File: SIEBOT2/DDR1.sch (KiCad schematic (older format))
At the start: 17 parts, among them U2 MT46V32M16TG, U3 M25P32

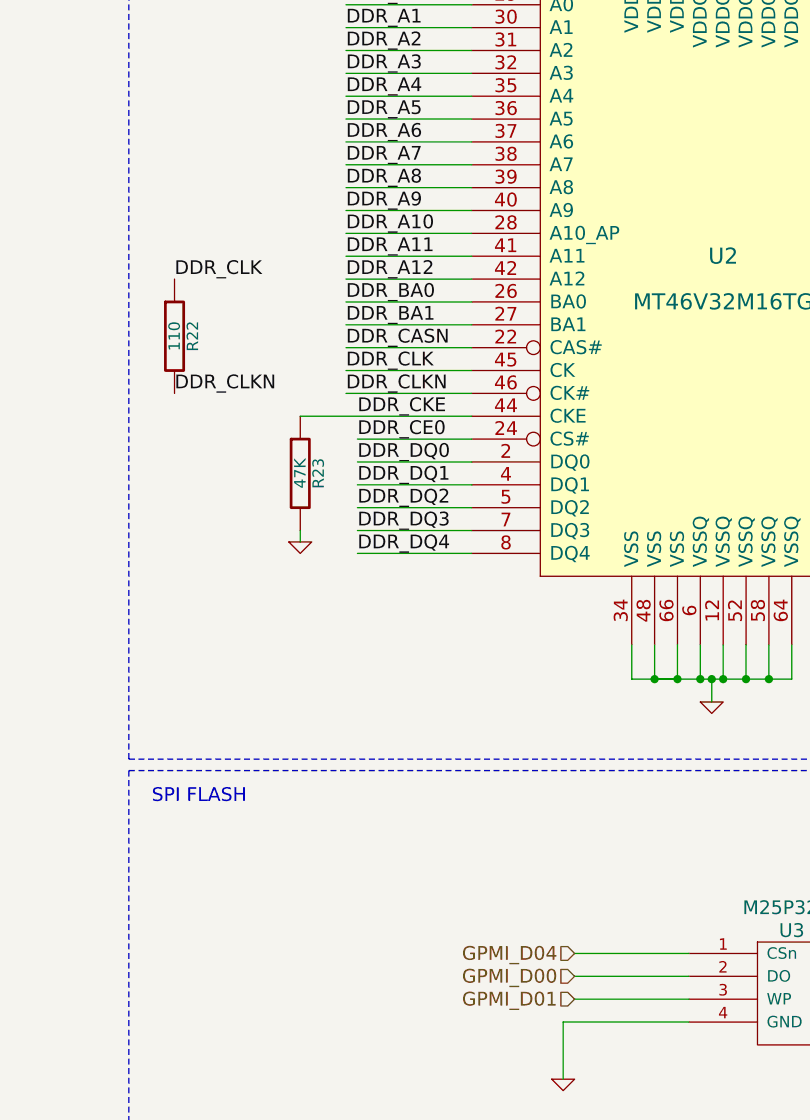
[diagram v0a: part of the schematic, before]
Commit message: Added some fixes from AndroidStamp
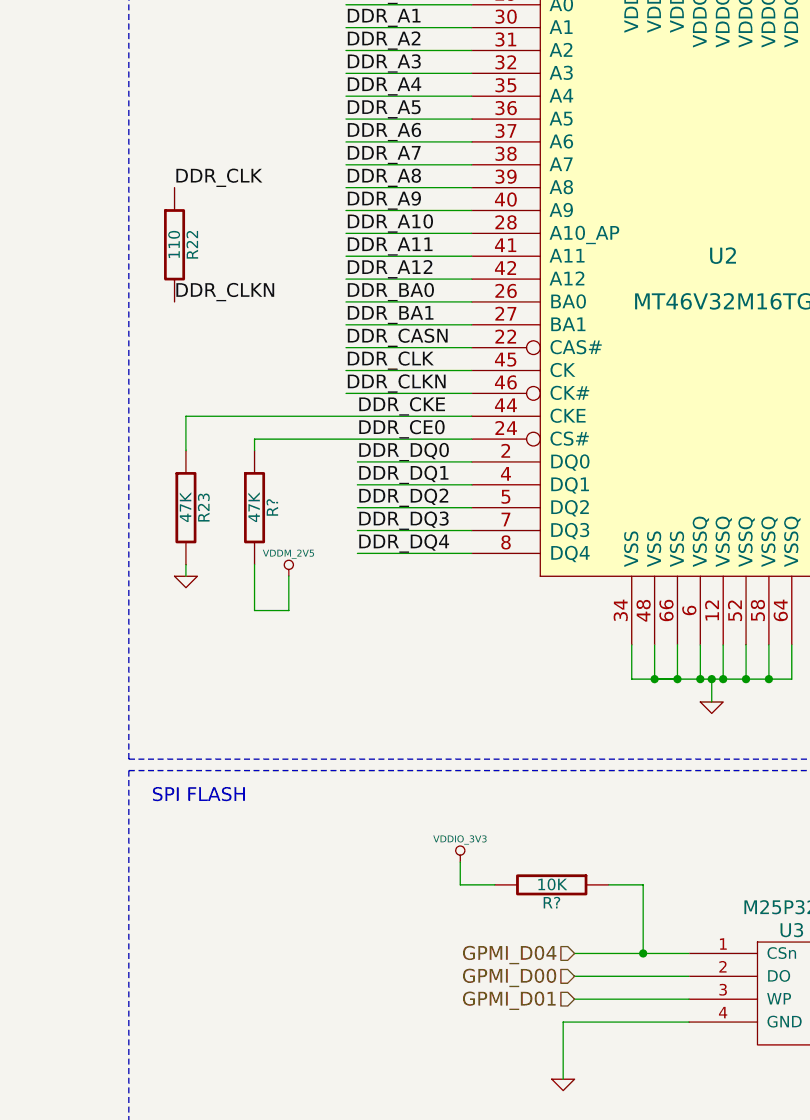
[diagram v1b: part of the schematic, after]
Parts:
- added R?: 47K, symbol R
- added R?: 10K, symbol R
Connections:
- wire segments 136 -> 145
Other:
- moved on the sheet: R22, R23
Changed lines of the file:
@@
-EESchema Schematic File Version 2  date sáb 05 mar 2011 23:35:11 COT
+EESchema Schematic File Version 2  date jue 07 abr 2011 23:57:53 COT
 LIBS:stm32f100vxx
 LIBS:transistor-npn
@@
 LIBS:PROpendous-cache
 LIBS:w_analog
+LIBS:adm3101e
 LIBS:i.mx233stamp-cache
 EELAYER 25  0
@@
 Sheet 5 6
 Title ""
-Date "6 mar 2011"
+Date "8 apr 2011"
 Rev ""
 Comp ""
@@
 Comment4 ""
 $EndDescr
-Text Notes 5850 5500 0    60   ~ 0
-SPI FLASH
+Wire Wire Line
+	7700 6250 8200 6250
+Connection ~ 8000 6150
+Wire Wire Line
+	8000 6150 8000 5850
+Wire Wire Line
+	8000 5850 7850 5850
+Wire Wire Line
+	7250 3900 6300 3900
+Wire Wire Line
+	6300 3900 6300 3950
 Wire Notes Line
 	5750 5350 5750 7150
@@
 Wire Wire Line
 	6700 3300 7250 3300
-Wire Wire Line
-	7250 3800 6500 3800
 Connection ~ 10800 1500
 Wire Wire Line
@@
 Connection ~ 9600 950
 Connection ~ 9900 950
-Wire Wire Line
-	9850 6350 9350 6350
 Wire Wire Line
 	9700 6000 9700 6150
@@
 Connection ~ 8450 1500
 Wire Wire Line
-	7700 6250 8200 6250
-Wire Wire Line
 	8200 6450 7650 6450
 Wire Wire Line
@@
 Connection ~ 10800 2700
 Wire Wire Line
-	6500 4300 6500 4350
+	6000 4450 6000 4500
 Wire Wire Line
 	6700 3400 7250 3400
@@
 	6700 3600 7250 3600
 Wire Wire Line
-	6750 3900 7250 3900
-Wire Wire Line
 	9450 3400 10000 3400
 Wire Wire Line
@@
 Wire Notes Line
 	11150 7150 5750 7150
+Wire Wire Line
+	6000 3950 6000 3800
+Wire Wire Line
+	6000 3800 7250 3800
+Wire Wire Line
+	6300 4450 6300 4650
+Wire Wire Line
+	6300 4650 6450 4650
+Wire Wire Line
+	6450 4650 6450 4500
+Wire Wire Line
+	7200 5750 7200 5850
+Wire Wire Line
+	7200 5850 7350 5850
+Wire Wire Line
+	9850 6350 9350 6350
+$Comp
+L VDDIO_3V3 #PWR?
+U 1 1 4D7D59A9
+P 7200 5750
+F 0 "#PWR?" H 7200 5850 30  0001 C CNN
+F 1 "VDDIO_3V3" H 7200 5850 30  0000 C CNN
+	1    7200 5750
+	1    0    0    -1
+$EndComp
+$Comp
+L R R?
+U 1 1 4D7D5980
+P 7600 5850
+F 0 "R?" V 7680 5850 50  0000 C CNN
+F 1 "10K" V 7600 5850 50  0000 C CNN
+	1    7600 5850
+	0    1    1    0
+$EndComp
+$Comp
+L VDDM_2V5 #PWR?
+U 1 1 4D7D4B15
+P 6450 4500
+F 0 "#PWR?" H 6450 4600 30  0001 C CNN
+F 1 "VDDM_2V5" H 6450 4600 30  0000 C CNN
+	1    6450 4500
+	1    0    0    -1
+$EndComp
+$Comp
+L R R?
+U 1 1 4D7D4AD6
+P 6300 4200
+F 0 "R?" V 6380 4200 50  0000 C CNN
+F 1 "47K" V 6300 4200 50  0000 C CNN
+	1    6300 4200
+	1    0    0    -1
+$EndComp
+Text Notes 5850 5500 0    60   ~ 0
+SPI FLASH
 Text Notes 5850 750  0    60   ~ 0
 DDR RAM
-Text Label 5950 3700 0    60   ~ 0
+Text Label 5950 3300 0    60   ~ 0
 DDR_CLKN
-Text Label 5950 3200 0    60   ~ 0
+Text Label 5950 2800 0    60   ~ 0
 DDR_CLK
 $Comp
 L R R22
 U 1 1 4D41DFB8
-P 5950 3450
-F 0 "R22" V 6030 3450 50  0000 C CNN
-F 1 "110" V 5950 3450 50  0000 C CNN
-	1    5950 3450
+P 5950 3050
+F 0 "R22" V 6030 3050 50  0000 C CNN
+F 1 "110" V 5950 3050 50  0000 C CNN
+	1    5950 3050
 	1    0    0    -1
 $EndComp
@@
 L R R23
 U 1 1 4D418363
-P 6500 4050
-F 0 "R23" V 6580 4050 50  0000 C CNN
-F 1 "47K" V 6500 4050 50  0000 C CNN
-	1    6500 4050
+P 6000 4200
+F 0 "R23" V 6080 4200 50  0000 C CNN
+F 1 "47K" V 6000 4200 50  0000 C CNN
+	1    6000 4200
 	1    0    0    -1
 $EndComp
@@
 L GND #PWR01
 U 1 1 4D418353
-P 6500 4350
-F 0 "#PWR01" H 6500 4350 30  0001 C CNN
-F 1 "GND" H 6500 4280 30  0001 C CNN
-	1    6500 4350
+P 6000 4500
+F 0 "#PWR01" H 6000 4500 30  0001 C CNN
+F 1 "GND" H 6000 4430 30  0001 C CNN
+	1    6000 4500
 	1    0    0    -1
 $EndComp

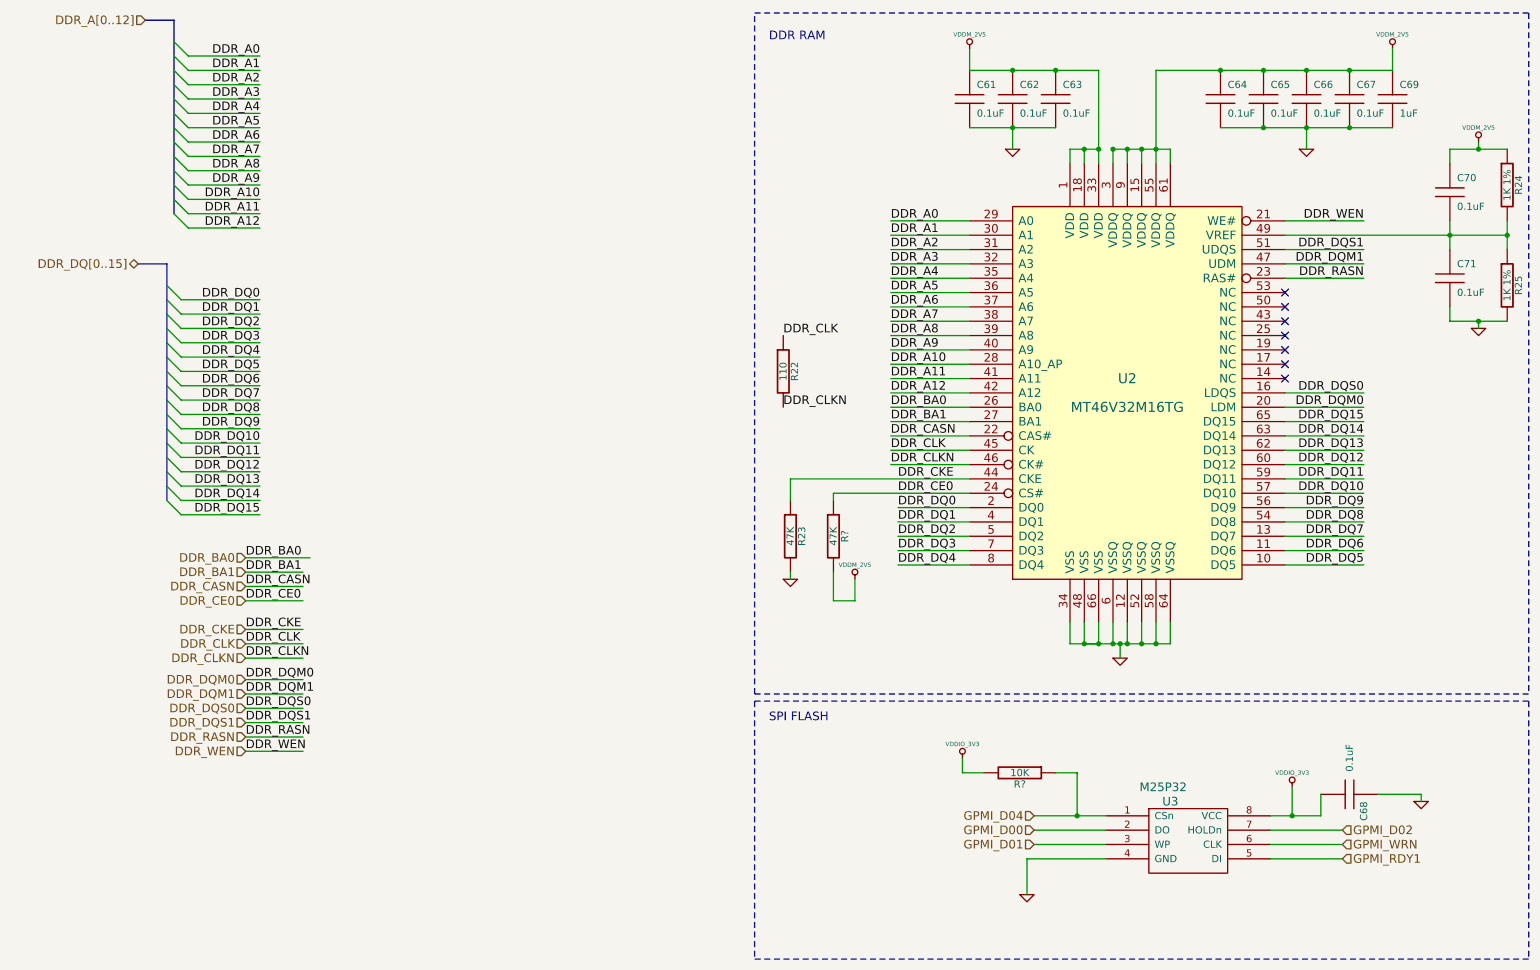
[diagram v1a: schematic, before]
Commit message: Added power dc-dc, fixed stm32 control pins
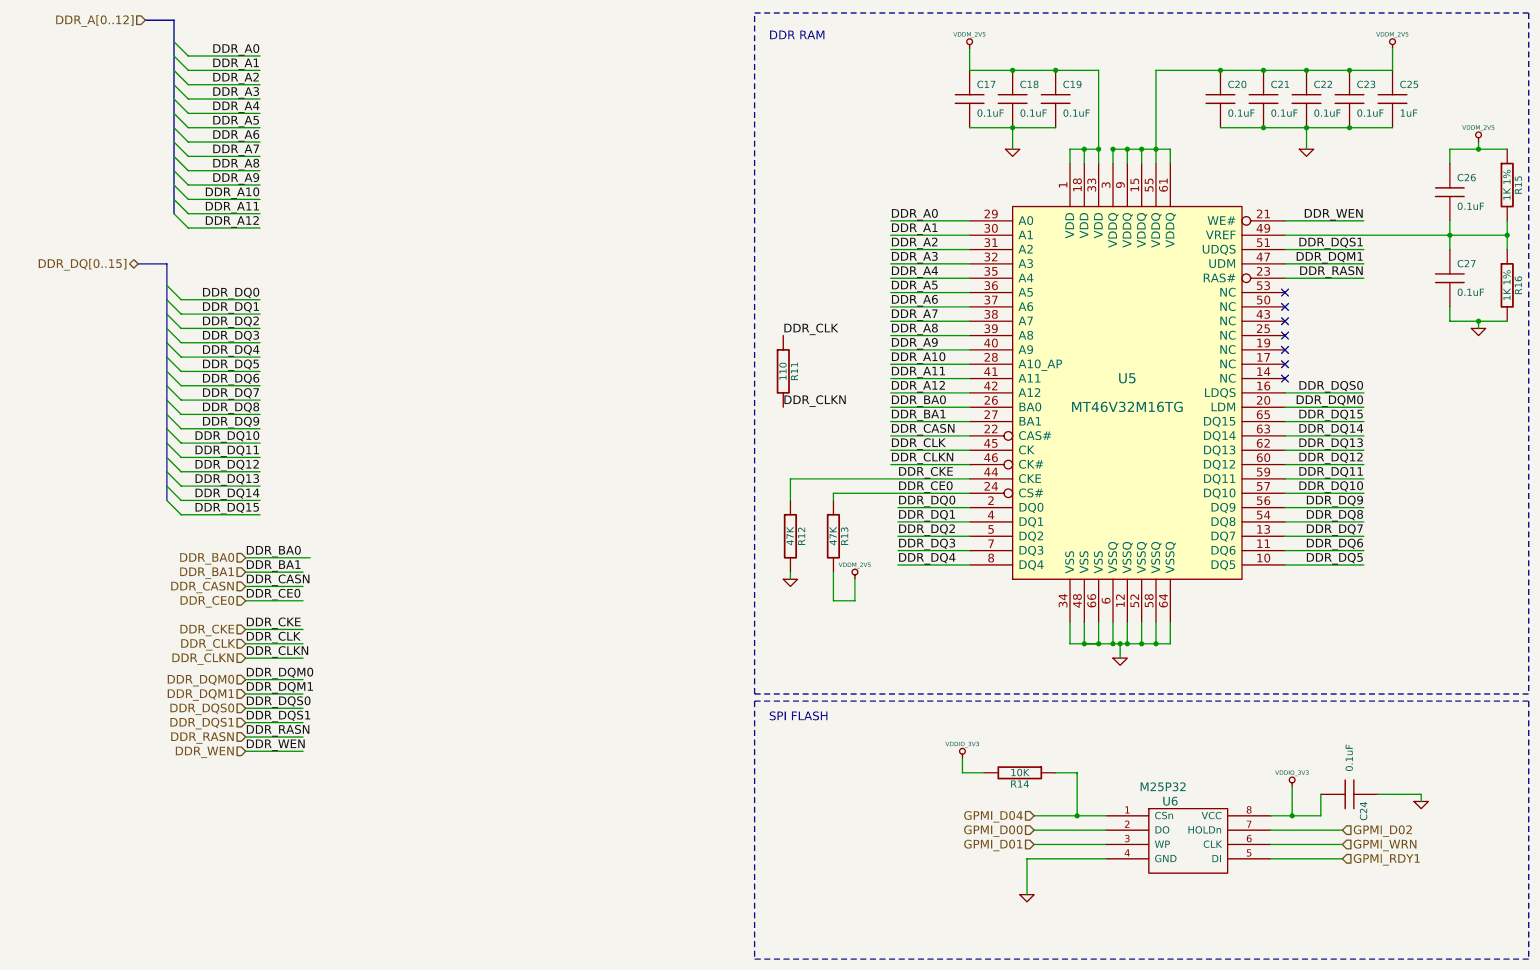
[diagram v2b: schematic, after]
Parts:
- gave numbers to parts that had none: 2
- renumbered C61 to C17, C62 to C18, C63 to C19, C64 to C20, C65 to C21, C66 to C22, C67 to C23, C68 to C24, C69 to C25, C70 to C26, C71 to C27, R22 to R11, R23 to R12, R24 to R15, R25 to R16, U2 to U5, U3 to U6
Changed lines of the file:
@@
-EESchema Schematic File Version 2  date jue 07 abr 2011 23:57:53 COT
+EESchema Schematic File Version 2  date lun 11 abr 2011 13:13:06 COT
+LIBS:dc-dc
 LIBS:stm32f100vxx
 LIBS:transistor-npn
@@
 Sheet 5 6
 Title ""
-Date "8 apr 2011"
+Date "11 apr 2011"
 Rev ""
 Comp ""
@@
 	9850 6350 9350 6350
 $Comp
-L VDDIO_3V3 #PWR?
+L VDDIO_3V3 #PWR049
 U 1 1 4D7D59A9
 P 7200 5750
-F 0 "#PWR?" H 7200 5850 30  0001 C CNN
+F 0 "#PWR049" H 7200 5850 30  0001 C CNN
 F 1 "VDDIO_3V3" H 7200 5850 30  0000 C CNN
 	1    7200 5750
@@
 $EndComp
 $Comp
-L R R?
+L R R14
 U 1 1 4D7D5980
 P 7600 5850
-F 0 "R?" V 7680 5850 50  0000 C CNN
+F 0 "R14" V 7680 5850 50  0000 C CNN
 F 1 "10K" V 7600 5850 50  0000 C CNN
 	1    7600 5850
@@
 $EndComp
 $Comp
-L VDDM_2V5 #PWR?
+L VDDM_2V5 #PWR050
 U 1 1 4D7D4B15
 P 6450 4500
-F 0 "#PWR?" H 6450 4600 30  0001 C CNN
+F 0 "#PWR050" H 6450 4600 30  0001 C CNN
 F 1 "VDDM_2V5" H 6450 4600 30  0000 C CNN
 	1    6450 4500
@@
 $EndComp
 $Comp
-L R R?
+L R R13
 U 1 1 4D7D4AD6
 P 6300 4200
-F 0 "R?" V 6380 4200 50  0000 C CNN
+F 0 "R13" V 6380 4200 50  0000 C CNN
 F 1 "47K" V 6300 4200 50  0000 C CNN
 	1    6300 4200
@@
 DDR_CLK
 $Comp
-L R R22
+L R R11
 U 1 1 4D41DFB8
 P 5950 3050
-F 0 "R22" V 6030 3050 50  0000 C CNN
+F 0 "R11" V 6030 3050 50  0000 C CNN
 F 1 "110" V 5950 3050 50  0000 C CNN
 	1    5950 3050
@@
 DDR_CASN
 $Comp
-L R R23
+L R R12
 U 1 1 4D418363
 P 6000 4200
-F 0 "R23" V 6080 4200 50  0000 C CNN
+F 0 "R12" V 6080 4200 50  0000 C CNN
 F 1 "47K" V 6000 4200 50  0000 C CNN
 	1    6000 4200
@@
 $EndComp
 $Comp
-L GND #PWR01
+L GND #PWR051
 U 1 1 4D418353
 P 6000 4500
-F 0 "#PWR01" H 6000 4500 30  0001 C CNN
+F 0 "#PWR051" H 6000 4500 30  0001 C CNN
 F 1 "GND" H 6000 4430 30  0001 C CNN
 	1    6000 4500
@@
 DDR_CKE
 $Comp
-L GND #PWR02
+L GND #PWR052
 U 1 1 4D417AF1
 P 10800 2750
-F 0 "#PWR02" H 10800 2750 30  0001 C CNN
+F 0 "#PWR052" H 10800 2750 30  0001 C CNN
 F 1 "GND" H 10800 2680 30  0001 C CNN
 	1    10800 2750
@@
 $EndComp
 $Comp
-L VDDM_2V5 #PWR03
+L VDDM_2V5 #PWR053
 U 1 1 4D417ACD
 P 10800 1450
-F 0 "#PWR03" H 10800 1550 30  0001 C CNN
+F 0 "#PWR053" H 10800 1550 30  0001 C CNN
 F 1 "VDDM_2V5" H 10800 1550 30  0000 C CNN
 	1    10800 1450
@@
 $EndComp
 $Comp
-L R R25
+L R R16
 U 1 1 4D417AA2
 P 11000 2450
-F 0 "R25" V 11080 2450 50  0000 C CNN
+F 0 "R16" V 11080 2450 50  0000 C CNN
 F 1 "1K 1%" V 11000 2450 50  0000 C CNN
 	1    11000 2450
@@
 $EndComp
 $Comp
-L R R24
+L R R15
 U 1 1 4D417A9C
 P 11000 1750
-F 0 "R24" V 11080 1750 50  0000 C CNN
+F 0 "R15" V 11080 1750 50  0000 C CNN
 F 1 "1K 1%" V 11000 1750 50  0000 C CNN
 	1    11000 1750
@@
 $EndComp
 $Comp
-L C C71
+L C C27
 U 1 1 4D417A94
 P 10600 2400
-F 0 "C71" H 10650 2500 50  0000 L CNN
+F 0 "C27" H 10650 2500 50  0000 L CNN
 F 1 "0.1uF" H 10650 2300 50  0000 L CNN
 	1    10600 2400
@@
 $EndComp
 $Comp
-L C C70
+L C C26
 U 1 1 4D417A8B
 P 10600 1800
-F 0 "C70" H 10650 1900 50  0000 L CNN
+F 0 "C26" H 10650 1900 50  0000 L CNN
 F 1 "0.1uF" H 10650 1700 50  0000 L CNN
 	1    10600 1800
@@
 $EndComp
 $Comp
-L VDDM_2V5 #PWR04
+L VDDM_2V5 #PWR054
 U 1 1 4D4179A4
 P 7250 800
-F 0 "#PWR04" H 7250 900 30  0001 C CNN
+F 0 "#PWR054" H 7250 900 30  0001 C CNN
 F 1 "VDDM_2V5" H 7250 900 30  0000 C CNN
 	1    7250 800
@@
 $EndComp
 $Comp
-L VDDM_2V5 #PWR05
+L VDDM_2V5 #PWR055
 U 1 1 4D417999
 P 10200 800
-F 0 "#PWR05" H 10200 900 30  0001 C CNN
+F 0 "#PWR055" H 10200 900 30  0001 C CNN
 F 1 "VDDM_2V5" H 10200 900 30  0000 C CNN
 	1    10200 800
@@
 $EndComp
 $Comp
-L GND #PWR06
+L GND #PWR056
 U 1 1 4D41792B
 P 7550 1500
-F 0 "#PWR06" H 7550 1500 30  0001 C CNN
+F 0 "#PWR056" H 7550 1500 30  0001 C CNN
 F 1 "GND" H 7550 1430 30  0001 C CNN
 	1    7550 1500
@@
 $EndComp
 $Comp
-L C C61
+L C C17
 U 1 1 4D417911
 P 7250 1150
-F 0 "C61" H 7300 1250 50  0000 L CNN
+F 0 "C17" H 7300 1250 50  0000 L CNN
 F 1 "0.1uF" H 7300 1050 50  0000 L CNN
 	1    7250 1150
@@
 $EndComp
 $Comp
-L C C62
+L C C18
 U 1 1 4D41790C
 P 7550 1150
-F 0 "C62" H 7600 1250 50  0000 L CNN
+F 0 "C18" H 7600 1250 50  0000 L CNN
 F 1 "0.1uF" H 7600 1050 50  0000 L CNN
 	1    7550 1150
@@
 $EndComp
 $Comp
-L C C63
+L C C19
 U 1 1 4D417905
 P 7850 1150
-F 0 "C63" H 7900 1250 50  0000 L CNN
+F 0 "C19" H 7900 1250 50  0000 L CNN
 F 1 "0.1uF" H 7900 1050 50  0000 L CNN
 	1    7850 1150
@@
 $EndComp
 $Comp
-L GND #PWR07
+L GND #PWR057
 U 1 1 4D417882
 P 9600 1500
-F 0 "#PWR07" H 9600 1500 30  0001 C CNN
+F 0 "#PWR057" H 9600 1500 30  0001 C CNN
 F 1 "GND" H 9600 1430 30  0001 C CNN
 	1    9600 1500
@@
 $EndComp
 $Comp
-L C C69
+L C C25
 U 1 1 4D417845
 P 10200 1150
-F 0 "C69" H 10250 1250 50  0000 L CNN
+F 0 "C25" H 10250 1250 50  0000 L CNN
 F 1 "1uF" H 10250 1050 50  0000 L CNN
 	1    10200 1150
@@
 $EndComp
 $Comp
-L C C67
+L C C23
 U 1 1 4D41783A
 P 9900 1150
-F 0 "C67" H 9950 1250 50  0000 L CNN
+F 0 "C23" H 9950 1250 50  0000 L CNN
 F 1 "0.1uF" H 9950 1050 50  0000 L CNN
 	1    9900 1150
@@
 $EndComp
 $Comp
-L C C66
+L C C22
 U 1 1 4D417834
 P 9600 1150
-F 0 "C66" H 9650 1250 50  0000 L CNN
+F 0 "C22" H 9650 1250 50  0000 L CNN
 F 1 "0.1uF" H 9650 1050 50  0000 L CNN
 	1    9600 1150
@@
 $EndComp
 $Comp
-L C C65
+L C C21
 U 1 1 4D41782F
 P 9300 1150
-F 0 "C65" H 9350 1250 50  0000 L CNN
+F 0 "C21" H 9350 1250 50  0000 L CNN
 F 1 "0.1uF" H 9350 1050 50  0000 L CNN
 	1    9300 1150
@@
 $EndComp
 $Comp
-L C C64
+L C C20
 U 1 1 4D417828
 P 9000 1150
-F 0 "C64" H 9050 1250 50  0000 L CNN
+F 0 "C20" H 9050 1250 50  0000 L CNN
 F 1 "0.1uF" H 9050 1050 50  0000 L CNN
 	1    9000 1150
@@
 GPMI_D04
 $Comp
-L GND #PWR08
+L GND #PWR058
 U 1 1 4D409664
 P 10400 6050
-F 0 "#PWR08" H 10400 6050 30  0001 C CNN
+F 0 "#PWR058" H 10400 6050 30  0001 C CNN
 F 1 "GND" H 10400 5980 30  0001 C CNN
 	1    10400 6050
@@
 $EndComp
 $Comp
-L C C68
+L C C24
 U 1 1 4D409658
 P 9900 6000
-F 0 "C68" H 9950 6100 50  0000 L CNN
+F 0 "C24" H 9950 6100 50  0000 L CNN
 F 1 "0.1uF" H 9550 6000 50  0000 L CNN
 	1    9900 6000
@@
 $EndComp
 $Comp
-L VDDIO_3V3 #PWR09
+L VDDIO_3V3 #PWR059
 U 1 1 4D409635
 P 9500 5950
-F 0 "#PWR09" H 9500 6050 30  0001 C CNN
+F 0 "#PWR059" H 9500 6050 30  0001 C CNN
 F 1 "VDDIO_3V3" H 9500 6050 30  0000 C CNN
 	1    9500 5950
@@
 $EndComp
 $Comp
-L GND #PWR010
+L GND #PWR060
 U 1 1 4D409619
 P 7650 6700
-F 0 "#PWR010" H 7650 6700 30  0001 C CNN
+F 0 "#PWR060" H 7650 6700 30  0001 C CNN
 F 1 "GND" H 7650 6630 30  0001 C CNN
 	1    7650 6700
@@
 $EndComp
 $Comp
-L M25P32 U3
+L M25P32 U6
 U 1 1 4D40953F
 P 8800 6200
-F 0 "U3" H 8650 6350 60  0000 C CNN
+F 0 "U6" H 8650 6350 60  0000 C CNN
 F 1 "M25P32" H 8600 6450 60  0000 C CNN
 	1    8800 6200
@@
 DDR_WEN
 $Comp
-L GND #PWR011
+L GND #PWR061
 U 1 1 4D319D50
 P 8300 5050
-F 0 "#PWR011" H 8300 5050 30  0001 C CNN
+F 0 "#PWR061" H 8300 5050 30  0001 C CNN
 F 1 "GND" H 8300 4980 30  0001 C CNN
 	1    8300 5050
@@
 	1700 750  1800 850
 $Comp
-L MT46V32M16TG U2
+L MT46V32M16TG U5
 U 1 1 4D30BA6E
 P 8350 3200
-F 0 "U2" H 8350 3300 70  0000 C CNN
+F 0 "U5" H 8350 3300 70  0000 C CNN
 F 1 "MT46V32M16TG" H 8350 3100 70  0000 C CNN
 F 2 "TSOP-66" H 8350 3200 60  0001 C CNN
